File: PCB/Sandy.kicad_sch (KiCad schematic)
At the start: 248 parts, among them J1 USB_C_Receptacle_USB2.0, J2 Conn_01x03, J3 Conn_01x02, J5 Conn_02x03_Odd_Even, U1 ATmega32U4-MU, U2 24LC64, Y1 16MHz

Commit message: レイアウト落とし込み。マトリクス変更（総当たり→COL2ROW）
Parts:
- removed D0, D1, D2, D3, D4, D42, D5, D50, D6, D7, D8, D9: D, Diode_SMD:D_SOD-123, symbol Device:D
- removed EXT_DP2, EXT_DP6: Conn_01x01, TestPoint:TestPoint_THTPad_D1.5mm_Drill0.7mm, symbol Connector_Generic:Conn_01x01
- removed JP1: SolderJumper_2_Open, Jumper:SolderJumper-2_P1.3mm_Open_Pad1.0x1.5mm, symbol Jumper:SolderJumper_2_Open
- removed LS1: Speaker, Buzzer_Beeper:Buzzer_Murata_PKMCS0909E4000-R1, symbol Device:Speaker
- removed R7: 1k, Resistor_SMD:R_0805_2012Metric_Pad1.15x1.40mm_HandSolder, symbol Device:R_Small
- removed Reserve_AUDIO1, Reserve_AUDIO2, Reserve_PB5, Reserve_PC7, Reserve_PD5, Reserve_PF0, Reserve_PF6, Reserve_PF7: Conn_01x01, TestPoint:TestPoint_THTPad_D1.0mm_Drill0.5mm, symbol Connector_Generic:Conn_01x01
- removed SW_BS2u1: SW_Push, MX_Alps_Hybrid:MXOnly-2U-Hotswap-guide, symbol Switch:SW_Push
- removed SW_CSPC2u1: SW_Push, MX_Alps_Hybrid:MXOnly-2U-Hotswap-ReversedStabilizers-guide, symbol Switch:SW_Push
- removed SW_LALT1.5u/MHEN1u1, SW_RALT1.5u1: SW_Push, MX_Alps_Hybrid:MXOnly-1.5U-Hotswap-guide, symbol Switch:SW_Push
- removed SW_LEFT1, SW_LWIN1u1, SW_narrowCTL1u1: SW_Push, MX_Alps_Hybrid:MXOnly-1U-Hotswap-guide, symbol Switch:SW_Push
- removed SW_LSPC2.25u1: SW_Push, MX_Alps_Hybrid:MXOnly-2.25U-Hotswap-guide, symbol Switch:SW_Push
- removed SW_narrowRALT1.25u1: SW_Push, MX_Alps_Hybrid:MXOnly-1.25U-Hotswap-guide, symbol Switch:SW_Push
- removed SW_narrowRWIN1.25u1: SW_Push, MX_Alps_Hybrid:MXOnly-1.25U-Hotswap-guide-Rotate, symbol Switch:SW_Push
- added SW_TAB1.25u1: SW_Push, MX_Alps_Hybrid:MXOnly-1.5U-Hotswap-guide, symbol Switch:SW_Push
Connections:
- net AUDIO2 is gone; now on net col6: U1.30 (PB6)
- net resv_PB5 is gone; now on net col5: U1.29 (PB5)
- net resv_PD5 is gone; now on net row3: U1.22 (PD5)
- net resv_PF0 is gone; now on net row7: U1.41 (PF0)
- net resv_PF6 is gone; now on net row8: U1.37 (PF6)
- net resv_PF7 is gone; now on net row9: U1.36 (PF7)
- net MISO: now also EXT_DP0.1 (Pin_1), SW_'1.1, SW_6.1, SW_;1.1, SW_;2.1, SW_B1.1, SW_Center1.1, SW_CenterL1u1.1, SW_[1.1, SW_]1.1, SW_`1.1; no longer D12.1 (K), D14.1 (K), D18.1 (K), D19.1 (K), D61.1 (K), D62.1 (K), D63.1 (K), D67.1 (K), EXT_P0.1 (Pin_1)
- net MOSI: now also EXT_DP4.1 (Pin_1), SW_4.1, SW_5.1, SW_C1.1, SW_F1.1, SW_G1.1, SW_LSPC2u1.1, SW_R1.1, SW_T1.1, SW_V1.1; no longer D24.1 (K), D28.1 (K), D29.1 (K), D30.1 (K), D71.1 (K), D73.1 (K), D75.1 (K), D78.1 (K), EXT_P1.1 (Pin_1)
- net RE1_1: now also U1.12 (PB7); no longer SW_-1.1, SW_BS1.25u1.1, SW_BS1.5u1.1, SW_DOWN1.1, SW_ENT1.25u1.1, SW_ENT1.5u1.1, SW_UP1.1, SW_]2.1, SW_narrow1u1.1
- net RE2_1: now also SW_L2-1u1.1, U1.8 (PB0), SW_TAB1.25u1.1
- net SCK: now also EXT_DP8.1 (Pin_1), SW_2.1, SW_3.1, SW_D1.1, SW_E1.1, SW_LALT1.25u1.1, SW_LWIN1.25u1.1, SW_S1.1, SW_W1.1, SW_X1.1, SW_Z1.1; no longer D23.1 (K), D25.1 (K), D26.1 (K), D27.1 (K), D69.1 (K), D74.1 (K), EXT_P6.1 (Pin_1)
- net col6: now reaches EXT_DP7.1 (Pin_1), SW_'2.1, SW_0.1, SW_;3.1, SW_>1.1, SW_ENT2.25u1.1, SW_P1.1, SW_ROPT1.25u1.1, SW_[2.1
- net col6: now also SW_-1.1, SW_BS1.25u1.1, SW_BS1.5u1.1, SW_DOWN1.1, SW_ENT1.25u1.1, SW_ENT1.5u1.1, SW_UP1.1, SW_]2.1, SW_narrow1u1.1
- net col4: now reaches SW_7.1, SW_J1.1, SW_N1.1, SW_RSPC2u1.1, SW_U1.1
- net col4: now also EXT_DP5.1 (Pin_1), SW_B2.1, SW_CenterR1u1.1, SW_H1.1, SW_Y1.1, SW_\1.1, U1.28 (PB4); no longer SW_8.1, SW_I1.1, SW_M1.1
- net col5: now reaches EXT_DP3.1 (Pin_1), SW_9.1, SW_<1.1, SW_BS1.25u2.1, SW_BS1.5u2.1, SW_ENT1.25u2.1, SW_ENT1.5u2.1, SW_K1.1, SW_L1.1, SW_O1.1, SW_RALT1.25u1.1
- net col5: now also SW_8.1, SW_I1.1, SW_M1.1
- net at D29.2 (A), SW_TAB1.5u1.2: now also SW_TAB1.25u1.2
- net AUDIO1 renamed row0
- net row0: now also D12.1 (K), D14.1 (K), D18.1 (K), D19.1 (K), D61.1 (K), D62.1 (K), D63.1 (K), D67.1 (K), EXT_P0.1 (Pin_1)
- net pin2 renamed row2
- net row2: now also U1.25 (PD4); no longer U1.1 (PE6)
- net pin3 renamed row3
- net row3: no longer U1.26 (PD6)
- net pin4 renamed row4
- net row4: now also U1.26 (PD6); no longer U1.25 (PD4)
- net pin5 renamed row5
- net row5: now also U1.27 (PD7); no longer U1.8 (PB0)
- net pin7 renamed row7
- net row7: no longer U1.12 (PB7)
- net pin8 renamed row8
- net row8: no longer U1.28 (PB4)
- net pin9 renamed row9
- net row9: no longer U1.27 (PD7)
- net resv_PC7 renamed row1
- net row1: now also D24.1 (K), D28.1 (K), D29.1 (K), D30.1 (K), D71.1 (K), D73.1 (K), D75.1 (K), D78.1 (K), EXT_P1.1 (Pin_1)
- new net row6: D23.1 (K), D25.1 (K), D26.1 (K), D27.1 (K), D69.1 (K), D74.1 (K), EXT_P6.1 (Pin_1), U1.1 (PE6)
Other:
- note removed: "RESERVED PINS"
- note removed: "SPEAKER"
- moved on the sheet: EXT_DP0, EXT_DP3, EXT_DP4, SW_CenterL1u1, SW_LALT1.25u1, SW_LSPC2u1, SW_RALT1.25u1

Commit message: レイアウト落とし込み。ロータリーエンコーダ反映
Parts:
- removed SW_'2, SW_[2, SW_]2, SW_narrow1u1: SW_Push, MX_Alps_Hybrid:MXOnly-1U-Hotswap-guide, symbol Switch:SW_Push
- removed SW_BS1.25u1: SW_Push, MX_Alps_Hybrid:MXOnly-1.25U-Hotswap-guide, symbol Switch:SW_Push
- removed SW_BS1.25u2, SW_ENT1.25u2: SW_Push, MX_Alps_Hybrid:MXOnly-1.25U-Hotswap-guide-Rotate, symbol Switch:SW_Push
- removed SW_BS1.5u2, SW_ENT1.5u2: SW_Push, MX_Alps_Hybrid:MXOnly-1.5U-Hotswap-guide-Rotate, symbol Switch:SW_Push
- removed SW_ENT2.25u1: SW_Push, MX_Alps_Hybrid:MXOnly-2.25U-Hotswap-LeftRotate-guide, symbol Switch:SW_Push
- removed SW_RE1, SW_RE2: Rotary_Encoder_Switch, locallib:RotaryEncoder_Alps_EC11K-Switch_Vertical_H20mm, symbol Sandy-rescue:Rotary_Encoder_Switch-Device
- added SW_RE_L1, SW_RE_L2, SW_RE_R1, SW_RE_R2: RotaryEncoder_Switch, symbol Device:RotaryEncoder_Switch
- renumbered SW_;3 to SW_;1, SW_;1 to SW_;3
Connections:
- net GND: now also SW_RE_L1.C, SW_RE_L2.C, SW_RE_R1.C, SW_RE_R2.C
- net MISO: now also SW_RE_L2.S1
- net RE_L2_2: now reaches D22.2 (A), SW_CenterL1u1.2
- net RE_L2_2: now also SW_RE_L2.S2
- net RE_R2_2: now reaches D40.2 (A), SW_CenterR1u1.2
- net RE_R2_2: now also SW_RE_R2.S2
- net RE1_1 renamed RE_R1_1
- net RE_R1_1: now also SW_RE_R1.S1
- net RE1_2 renamed RE_R1_2
- net RE_R1_2: now also SW_RE_R1.S2
- net RE1_A renamed RE_L_A
- net RE_L_A: now also SW_RE_L1.A, SW_RE_L2.A
- net RE1_B renamed RE_L_B
- net RE_L_B: now also SW_RE_L1.B, SW_RE_L2.B
- net RE2_1 renamed RE_L1_1
- net RE_L1_1: now also SW_RE_L1.S1
- net RE2_2 renamed RE_L1_2
- net RE_L1_2: now also SW_RE_L1.S2
- net RE2_A renamed RE_R_A
- net RE_R_A: now also SW_RE_R1.A, SW_RE_R2.A
- net RE2_B renamed RE_R_B
- net RE_R_B: now also SW_RE_R1.B, SW_RE_R2.B
- net col4 renamed RE_R2_1
- net RE_R2_1: now also SW_RE_R2.S1

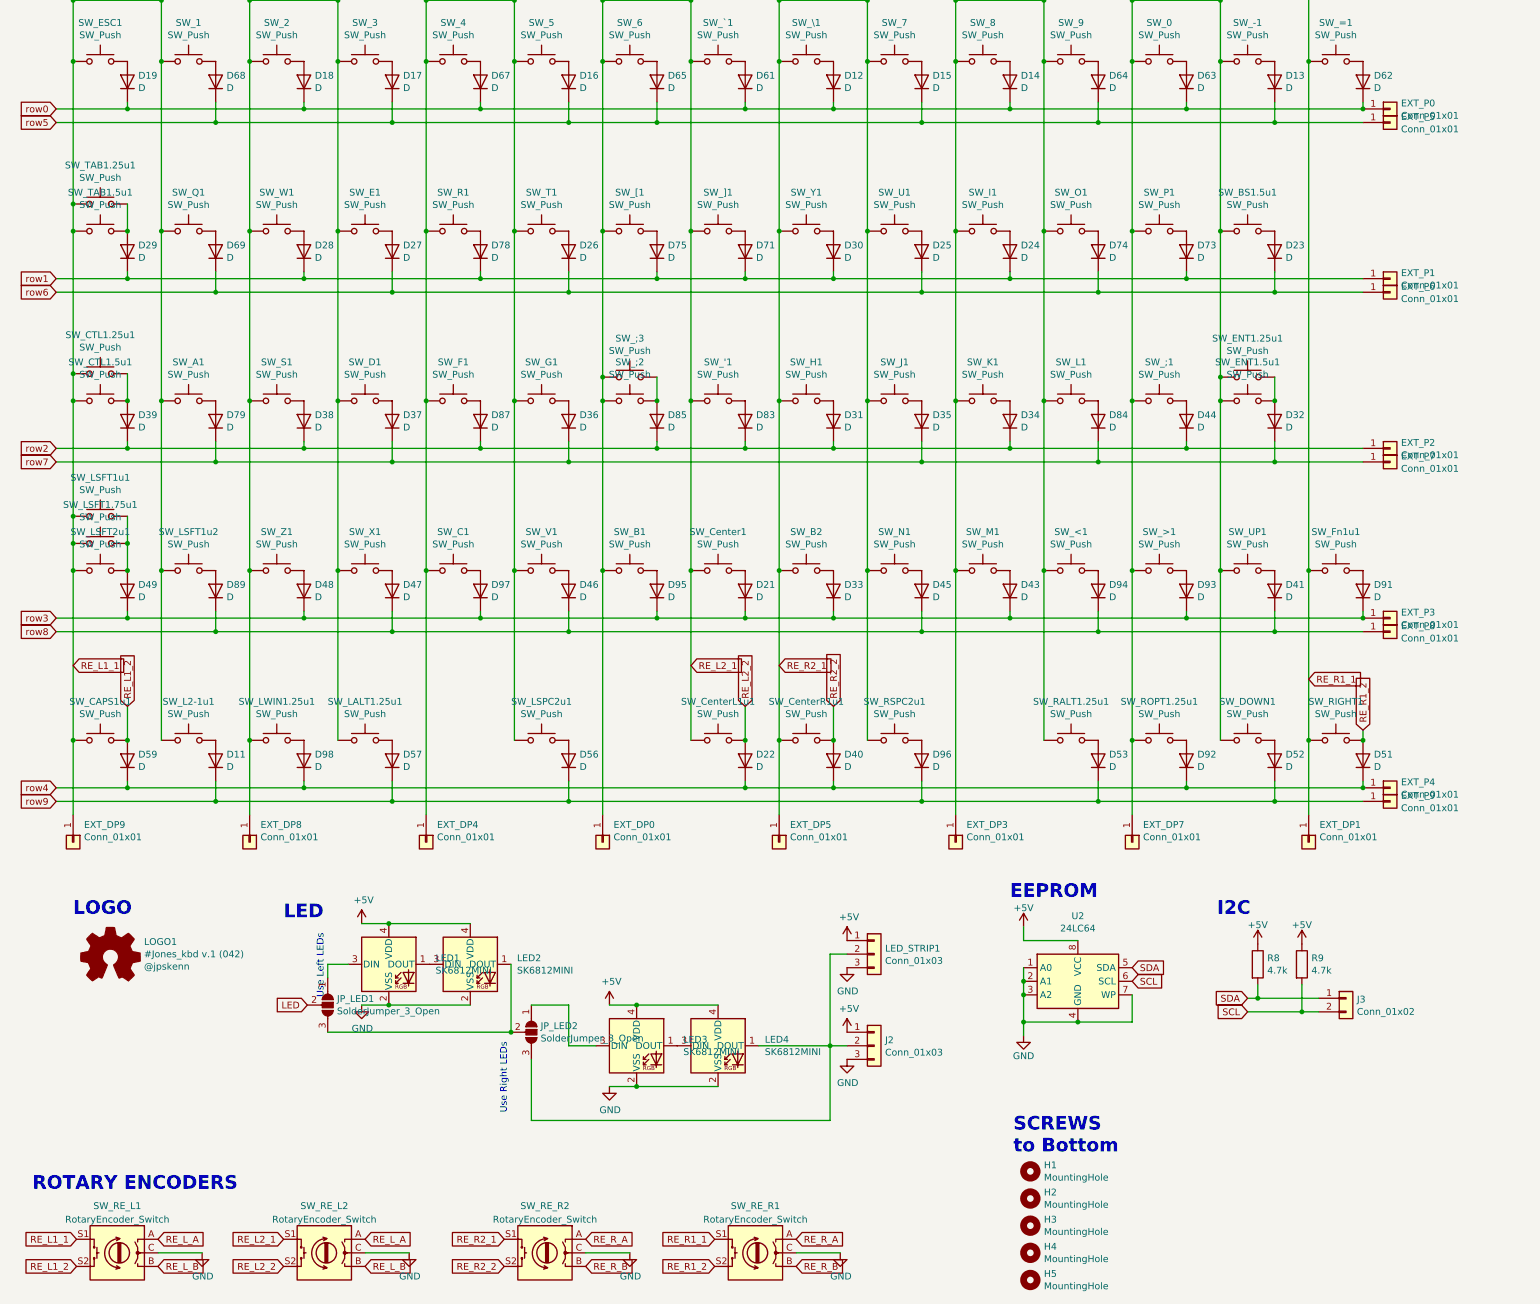
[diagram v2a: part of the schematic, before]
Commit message: テストピンなどを配置
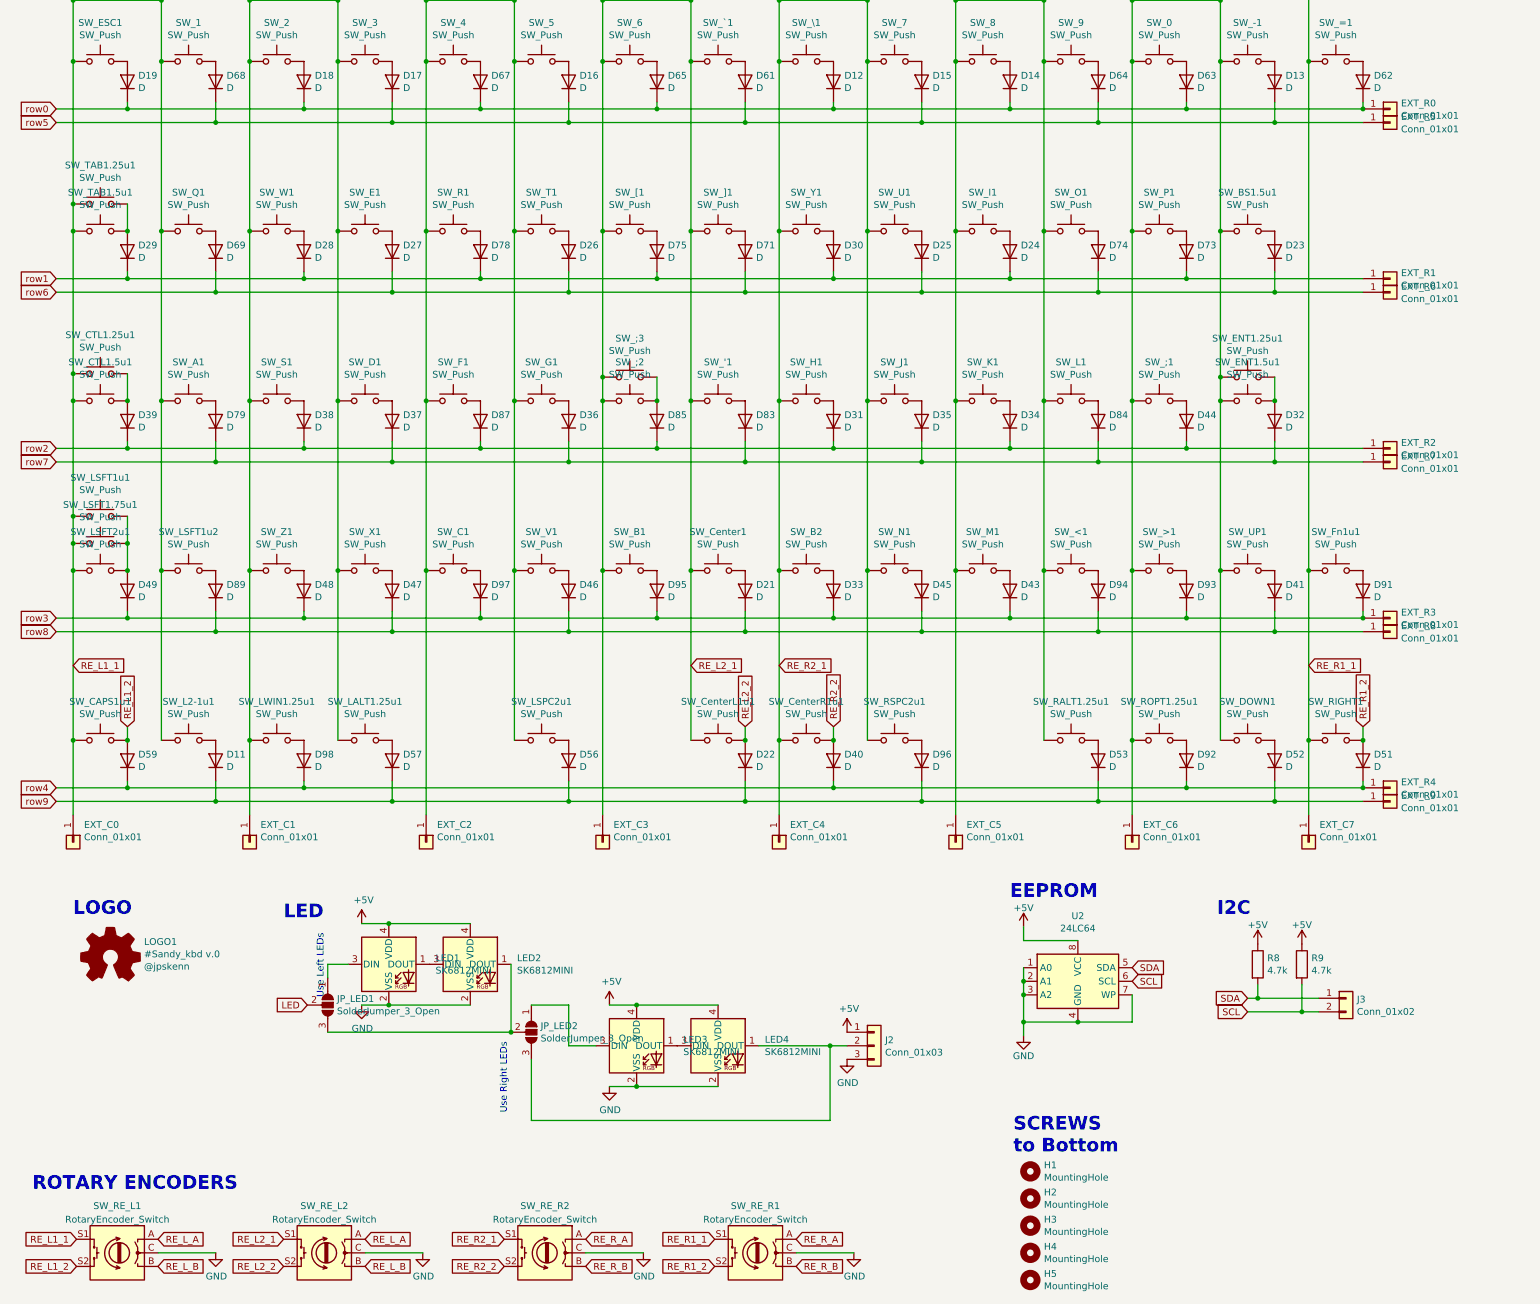
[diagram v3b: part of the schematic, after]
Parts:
- removed LED_STRIP1: Conn_01x03, locallib:LED_Strip, symbol Connector_Generic:Conn_01x03
- LOGO1: value #Jones_kbd v.1 (042) -> #Sandy_kbd v.0
- renumbered EXT_DP9 to EXT_C0, EXT_DP8 to EXT_C1, EXT_DP4 to EXT_C2, EXT_DP0 to EXT_C3, EXT_DP5 to EXT_C4, EXT_DP3 to EXT_C5, EXT_DP7 to EXT_C6, EXT_DP1 to EXT_C7, EXT_P0 to EXT_R0, EXT_P1 to EXT_R1, EXT_P2 to EXT_R2, EXT_P3 to EXT_R3, EXT_P4 to EXT_R4, EXT_P5 to EXT_R5, EXT_P6 to EXT_R6, EXT_P7 to EXT_R7, EXT_P8 to EXT_R8, EXT_P9 to EXT_R9
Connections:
- net row0: now also D65.1 (K); no longer D61.1 (K)
- net row1: no longer D71.1 (K)
- net row2: no longer D83.1 (K)
- net row3: no longer D21.1 (K)
- net row4: no longer D22.1 (K)
- net row5: now also D61.1 (K); no longer D65.1 (K)
- net row6: now also D71.1 (K)
- net row7: now also D83.1 (K)
- net row8: now also D21.1 (K)
- net row9: now also D22.1 (K)

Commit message: 子基板との接続を仮作成
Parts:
- added #J10, #J11, #J12, #J13, #J14, #J6, #J8, #J9: Conn_02x04_Row_Letter_Last, symbol Connector_Generic:Conn_02x04_Row_Letter_Last
- added #J2, #J3, #J4, #J5: Conn_02x08_Row_Letter_Last, symbol Connector_Generic:Conn_02x08_Row_Letter_Last
- added J10, J11, J12, J13, J14, J15, J8, J9: Conn_01x08, symbol Connector_Generic:Conn_01x08
- added J16, J17, J18, J19, J20, J21, J22, J23, J24, J25, J26, J27, J28, J29, J30, J31: Conn_01x04, symbol Connector_Generic:Conn_01x04
- SW_RE_L1, SW_RE_L2, SW_RE_R1, SW_RE_R2: footprint (none) -> locallib:RotaryEncoder_Alps_EC11K-Switch_Vertical_H20mm
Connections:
- net MISO: now also #J2.8a (Pin_8a), #J3.8a (Pin_8a), J10.8 (Pin_8), J8.8 (Pin_8)
- net MOSI: now also #J2.7a (Pin_7a), #J3.7a (Pin_7a), J10.7 (Pin_7), J8.7 (Pin_7)
- net RE_L1_1: now also #J2.5a (Pin_5a), #J3.5a (Pin_5a), J10.5 (Pin_5), J8.5 (Pin_5)
- net RE_R1_1: now also #J4.8a (Pin_8a), #J5.8a (Pin_8a), J12.8 (Pin_8), J14.8 (Pin_8)
- net RE_R2_1: now also #J4.5a (Pin_5a), #J5.5a (Pin_5a), #J6.3a (Pin_3a), #J8.3a (Pin_3a), J12.5 (Pin_5), J14.5 (Pin_5), J16.3 (Pin_3), J18.3 (Pin_3)
- net SCK: now also #J2.6a (Pin_6a), #J3.6a (Pin_6a), J10.6 (Pin_6), J8.6 (Pin_6)
- net col5: now also #J4.6a (Pin_6a), #J5.6a (Pin_6a), #J6.4a (Pin_4a), #J8.4a (Pin_4a), J12.6 (Pin_6), J14.6 (Pin_6), J16.4 (Pin_4), J18.4 (Pin_4)
- net col6: now also #J4.7a (Pin_7a), #J5.7a (Pin_7a), J12.7 (Pin_7), J14.7 (Pin_7)
- net row0: now also #J2.1a (Pin_1a), #J3.1a (Pin_1a), J10.1 (Pin_1), J8.1 (Pin_1)
- net row1: now also #J13.1a (Pin_1a), #J14.1a (Pin_1a), #J2.3a (Pin_3a), #J3.3a (Pin_3a), J10.3 (Pin_3), J28.1 (Pin_1), J30.1 (Pin_1), J8.3 (Pin_3)
- net row2: now also #J4.1a (Pin_1a), #J5.1a (Pin_1a), J12.1 (Pin_1), J14.1 (Pin_1)
- net row3: now also #J4.3a (Pin_3a), #J5.3a (Pin_3a), J12.3 (Pin_3), J14.3 (Pin_3)
- net row4: now also #J6.1a (Pin_1a), #J8.1a (Pin_1a), J16.1 (Pin_1), J18.1 (Pin_1)
- net row5: now also #J2.2a (Pin_2a), #J3.2a (Pin_2a), J10.2 (Pin_2), J8.2 (Pin_2)
- net row6: now also #J13.2a (Pin_2a), #J14.2a (Pin_2a), #J2.4a (Pin_4a), #J3.4a (Pin_4a), J10.4 (Pin_4), J28.2 (Pin_2), J30.2 (Pin_2), J8.4 (Pin_4)
- net row7: now also #J4.2a (Pin_2a), #J5.2a (Pin_2a), J12.2 (Pin_2), J14.2 (Pin_2)
- net row8: now also #J4.4a (Pin_4a), #J5.4a (Pin_4a), J12.4 (Pin_4), J14.4 (Pin_4)
- net row9: now also #J6.2a (Pin_2a), #J8.2a (Pin_2a), J16.2 (Pin_2), J18.2 (Pin_2)
- new net Mid_col0: #J10.1a (Pin_1a), #J2.5b (Pin_5b), #J3.5b (Pin_5b), #J9.3a (Pin_3a), J11.5 (Pin_5), J20.3 (Pin_3), J22.1 (Pin_1), J9.5 (Pin_5)
- new net Mid_col1: #J10.2a (Pin_2a), #J2.6b (Pin_6b), #J3.6b (Pin_6b), #J9.4a (Pin_4a), J11.6 (Pin_6), J20.4 (Pin_4), J22.2 (Pin_2), J9.6 (Pin_6)
- new net Mid_col2: #J10.3a (Pin_3a), #J13.3a (Pin_3a), #J2.7b (Pin_7b), #J3.7b (Pin_7b), J11.7 (Pin_7), J22.3 (Pin_3), J28.3 (Pin_3), J9.7 (Pin_7)
- new net Mid_col3: #J10.4a (Pin_4a), #J13.4a (Pin_4a), #J2.8b (Pin_8b), #J3.8b (Pin_8b), J11.8 (Pin_8), J22.4 (Pin_4), J28.4 (Pin_4), J9.8 (Pin_8)
- new net Mid_col4: #J11.1a (Pin_1a), #J14.3a (Pin_3a), #J4.5b (Pin_5b), #J5.5b (Pin_5b), #J6.3b (Pin_3b), #J8.3b (Pin_3b), J13.5 (Pin_5), J15.5 (Pin_5), J17.3 (Pin_3), J19.3 (Pin_3), J24.1 (Pin_1), J30.3 (Pin_3)
- new net Mid_col5: #J11.2a (Pin_2a), #J14.4a (Pin_4a), #J4.6b (Pin_6b), #J5.6b (Pin_6b), #J6.4b (Pin_4b), #J8.4b (Pin_4b), J13.6 (Pin_6), J15.6 (Pin_6), J17.4 (Pin_4), J19.4 (Pin_4), J24.2 (Pin_2), J30.4 (Pin_4)
- new net Mid_col6: #J11.3a (Pin_3a), #J12.3a (Pin_3a), #J4.7b (Pin_7b), #J5.7b (Pin_7b), J13.7 (Pin_7), J15.7 (Pin_7), J24.3 (Pin_3), J26.3 (Pin_3)
- new net Mid_col7: #J11.4a (Pin_4a), #J12.4a (Pin_4a), #J4.8b (Pin_8b), #J5.8b (Pin_8b), J13.8 (Pin_8), J15.8 (Pin_8), J24.4 (Pin_4), J26.4 (Pin_4)
- new net Mid_row0: #J12.1a (Pin_1a), #J2.1b (Pin_1b), #J3.1b (Pin_1b), #J9.1a (Pin_1a), J11.1 (Pin_1), J20.1 (Pin_1), J26.1 (Pin_1), J9.1 (Pin_1)
- new net Mid_row1: #J2.3b (Pin_3b), #J3.3b (Pin_3b), J11.3 (Pin_3), J9.3 (Pin_3)
- new net Mid_row2: #J4.1b (Pin_1b), #J5.1b (Pin_1b), J13.1 (Pin_1), J15.1 (Pin_1)
- new net Mid_row3: #J4.3b (Pin_3b), #J5.3b (Pin_3b), J13.3 (Pin_3), J15.3 (Pin_3)
- new net Mid_row4: #J6.1b (Pin_1b), #J8.1b (Pin_1b), J17.1 (Pin_1), J19.1 (Pin_1)
- new net Mid_row5: #J12.2a (Pin_2a), #J2.2b (Pin_2b), #J3.2b (Pin_2b), #J9.2a (Pin_2a), J11.2 (Pin_2), J20.2 (Pin_2), J26.2 (Pin_2), J9.2 (Pin_2)
- new net Mid_row6: #J2.4b (Pin_4b), #J3.4b (Pin_4b), J11.4 (Pin_4), J9.4 (Pin_4)
- new net Mid_row7: #J4.2b (Pin_2b), #J5.2b (Pin_2b), J13.2 (Pin_2), J15.2 (Pin_2)
- new net Mid_row8: #J4.4b (Pin_4b), #J5.4b (Pin_4b), J13.4 (Pin_4), J15.4 (Pin_4)
- new net Mid_row9: #J6.2b (Pin_2b), #J8.2b (Pin_2b), J17.2 (Pin_2), J19.2 (Pin_2)
- new net Top_col0: #J10.1b (Pin_1b), #J9.3b (Pin_3b), J21.3 (Pin_3), J23.1 (Pin_1)
- new net Top_col1: #J10.2b (Pin_2b), #J9.4b (Pin_4b), J21.4 (Pin_4), J23.2 (Pin_2)
- new net Top_col2: #J10.3b (Pin_3b), #J13.3b (Pin_3b), J23.3 (Pin_3), J29.3 (Pin_3)
- new net Top_col3: #J10.4b (Pin_4b), #J13.4b (Pin_4b), J23.4 (Pin_4), J29.4 (Pin_4)
- new net Top_col4: #J11.1b (Pin_1b), #J14.3b (Pin_3b), J25.1 (Pin_1), J31.3 (Pin_3)
- new net Top_col5: #J11.2b (Pin_2b), #J14.4b (Pin_4b), J25.2 (Pin_2), J31.4 (Pin_4)
- new net Top_col6: #J11.3b (Pin_3b), #J12.3b (Pin_3b), J25.3 (Pin_3), J27.3 (Pin_3)
- new net Top_col7: #J11.4b (Pin_4b), #J12.4b (Pin_4b), J25.4 (Pin_4), J27.4 (Pin_4)
- new net Top_row0: #J12.1b (Pin_1b), #J9.1b (Pin_1b), J21.1 (Pin_1), J27.1 (Pin_1)
- new net Top_row1: #J13.1b (Pin_1b), #J14.1b (Pin_1b), J29.1 (Pin_1), J31.1 (Pin_1)
- new net Top_row5: #J12.2b (Pin_2b), #J9.2b (Pin_2b), J21.2 (Pin_2), J27.2 (Pin_2)
- new net Top_row6: #J13.2b (Pin_2b), #J14.2b (Pin_2b), J29.2 (Pin_2), J31.2 (Pin_2)
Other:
- note added: "KEY MATRIX, Base plate"
- note added: "Panel CONNECTOR Base to Middle"
- note added: "Panel CONNECTOR Middle to Top"
- note removed: "KEY MATRIX"
